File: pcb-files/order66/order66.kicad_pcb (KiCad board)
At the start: 2 copper layers, 228.6 x 123 mm, 212 parts, among them J1 NICEVIEW, J2 Pouch Battery Connector, J3 swd connector, J6 millmax connector, SW1 AUX1, SW10 Z, SW11 AUX7, SW12 2, SW13 W, SW14 S, SW15 X, SW16 LALT, SW17 3, SW18 E, SW19 D, SW2 ESC, SW20 C, SW21 GUI, SW22 4, SW23 R, SW24 F, SW25 V, SW26 RAISE, SW27 5, SW28 T, SW29 G, SW3 TAB, SW30 B, SW31 LSPACE, SW32 AUX2, SW33 6, SW34 Y, SW35 H, SW36 N, SW37 RSPACE, SW38 AUX3, SW39 7, SW4 CAPSLCK, SW40 U, SW41 J, SW42 M, SW43 LOWER, SW44 AUX4, SW45 8, SW46 I, SW47 K, SW48 ,<, SW49 LEFT, SW5 LSHIFT, SW50 9, SW51 O, SW52 L, SW53 .>, SW54 DOWN, SW55 AUX5, SW56 0, SW57 P, SW58 ;:, SW59 /?, SW6 LCTRL, SW60 UP, SW61 AUX6, SW62 BACKSPACE, SW63 BACKSLACH, SW64 ENTER, SW65 RSHIFT, SW66 RIGHT, SW67 RST, SW68 ON/OFF, SW7 1, SW8 Q, SW9 A, U1 NiceNano

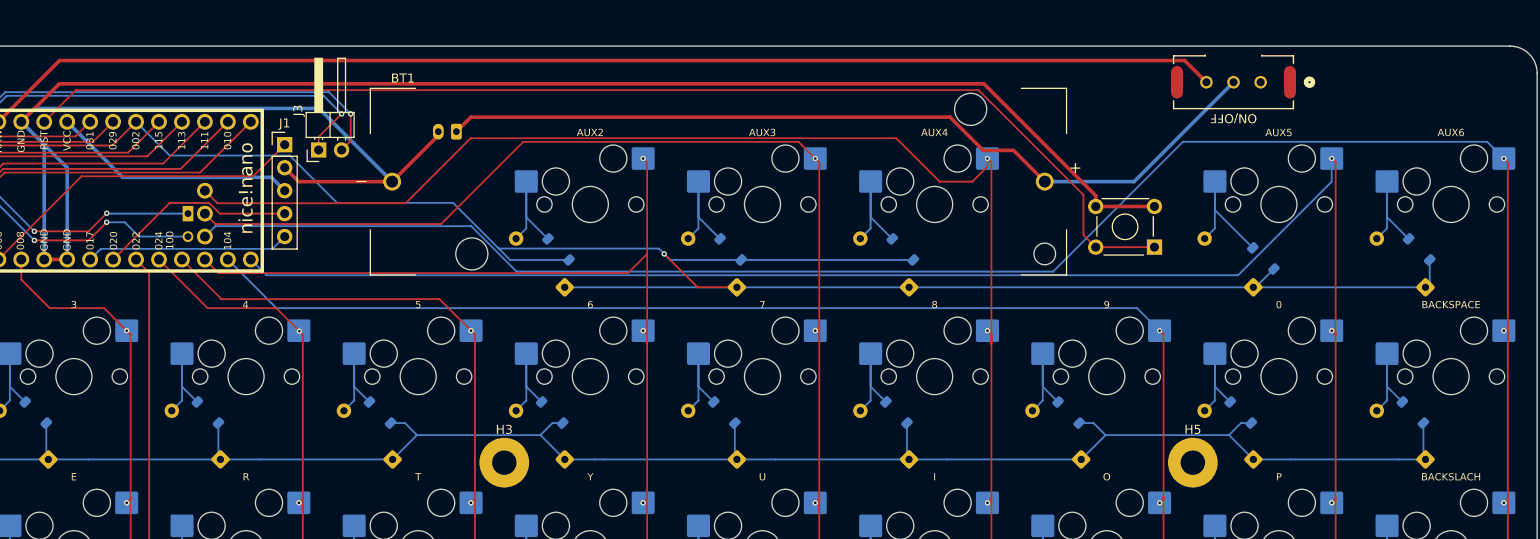
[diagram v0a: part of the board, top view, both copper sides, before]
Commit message: added the other version of power switch that I have as well just in case
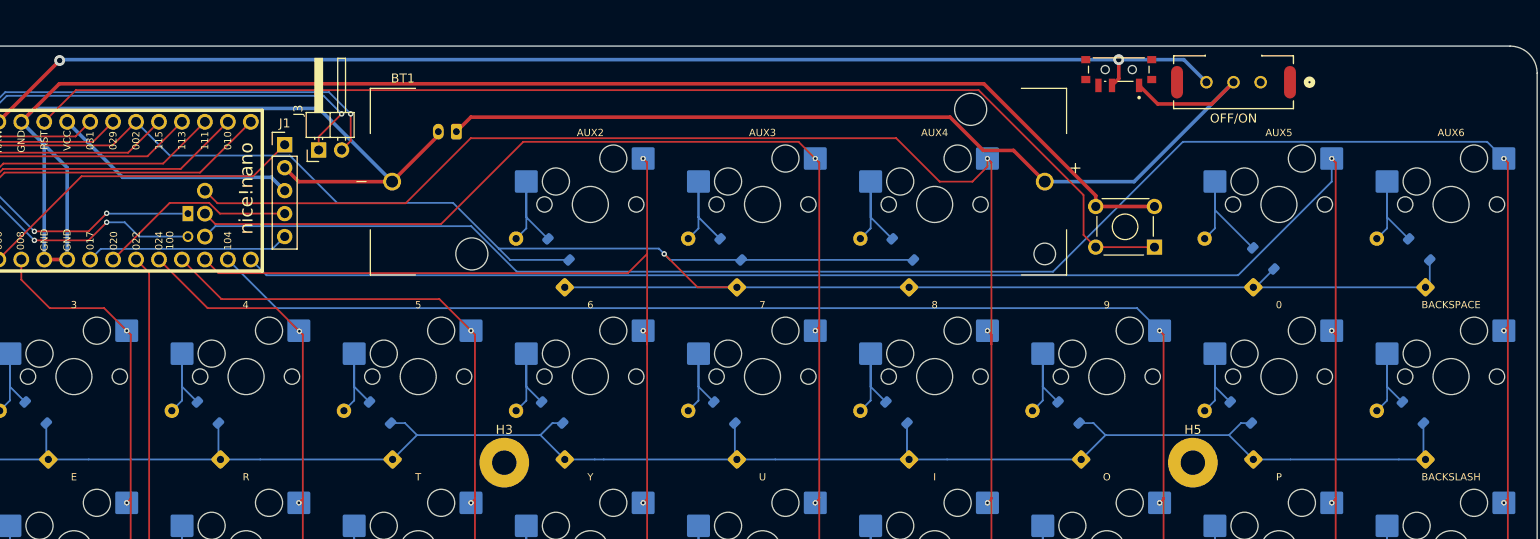
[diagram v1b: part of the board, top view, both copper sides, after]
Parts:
- added SW100: OFF/ON, SSSS811101:SW_SSSS811101, F.Cu at (272.1, 66.1)
- SW63: value BACKSLACH -> BACKSLASH
- SW68: value ON/OFF -> OFF/ON
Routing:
- net BATT+: track 94.3 -> 106.6 mm
- net VBATT+: track 137.5 -> 140.7 mm, vias 0 -> 2
